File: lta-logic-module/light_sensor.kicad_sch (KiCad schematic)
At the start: 9 parts

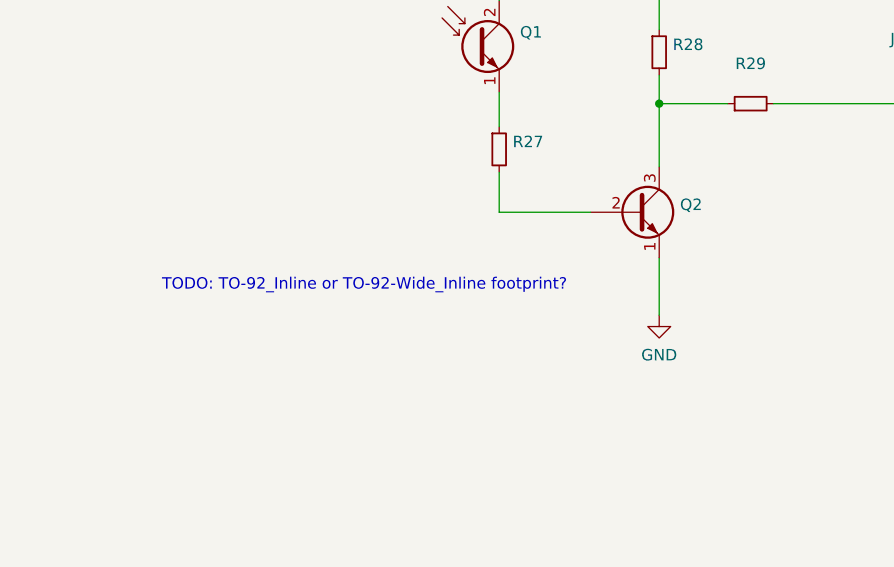
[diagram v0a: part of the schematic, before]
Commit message: Add main draft of PCB layout for logic module.
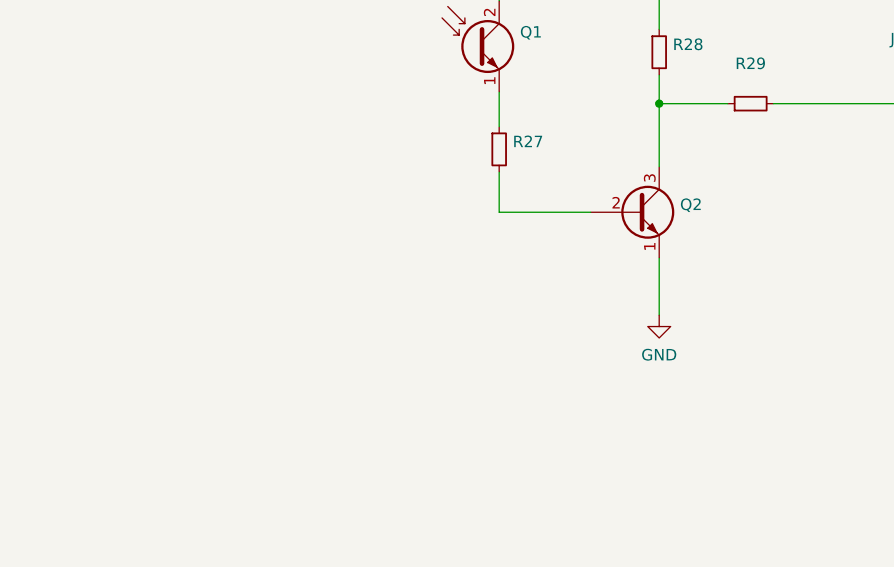
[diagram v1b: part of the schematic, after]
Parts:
- Q2: Comment (none) -> Any 2N3904 TO-92 transistor OK; MANUFACTURER onsemi -> Central Semiconductor; MPN KSC945CYTA -> 2N3904 PBFREE
- RV1: Comment (none) -> Any 25KOhm trimpot w/ same footprint OK
- SW1: Comment (none) -> Any 1x SPST THT dip switch w/ same footprint OK
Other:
- note removed: "TODO: TO-92_Inline or TO-92-Wide_Inline footprint?"
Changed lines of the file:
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@@
-    (effects (font (size 1.27 1.27)) (justify left bottom))
-  )
-  (text "TODO: TO-92_Inline or TO-92-Wide_Inline footprint?"
-    (at 36.83 76.835 0)
     (effects (font (size 1.27 1.27)) (justify left bottom))
   )
@@
     )
     (property "MANUFACTURER" "CUI Devices" (id 5) (at 122.555 34.925 90)
+      (effects (font (size 1.27 1.27)) hide)
+    )
+    (property "Comment" "Any 1x SPST THT dip switch w/ same footprint OK" (id 6) (at 122.555 34.925 0)
       (effects (font (size 1.27 1.27)) hide)
     )
@@
       (effects (font (size 1.27 1.27)) hide)
     )
-    (property "Datasheet" "https://www.onsemi.cn/pdf/datasheet/ksc945-d.pdf" (id 3) (at 89.535 67.945 0)
-      (effects (font (size 1.27 1.27)) hide)
-    )
-    (property "MPN" "KSC945CYTA" (id 4) (at 89.535 67.945 0)
-      (effects (font (size 1.27 1.27)) hide)
-    )
-    (property "MANUFACTURER" "onsemi" (id 5) (at 89.535 67.945 0)
+    (property "Datasheet" "" (id 3) (at 89.535 67.945 0)
+      (effects (font (size 1.27 1.27)) hide)
+    )
+    (property "MPN" "2N3904 PBFREE" (id 4) (at 89.535 67.945 0)
+      (effects (font (size 1.27 1.27)) hide)
+    )
+    (property "MANUFACTURER" "Central Semiconductor" (id 5) (at 89.535 67.945 0)
+      (effects (font (size 1.27 1.27)) hide)
+    )
+    (property "Comment" "Any 2N3904 TO-92 transistor OK" (id 6) (at 89.535 67.945 0)
       (effects (font (size 1.27 1.27)) hide)
     )
@@
   (symbol (lib_id "power:GND") (at 92.075 79.375 0) (unit 1)
     (in_bom yes) (on_board yes) (fields_autoplaced)
-    (property "Reference" "#PWR055" (id 0) (at 92.075 85.725 0)
+    (property "Reference" "#PWR056" (id 0) (at 92.075 85.725 0)
       (effects (font (size 1.27 1.27)) hide)
     )
@@
       (effects (font (size 1.27 1.27)) hide)
     )
+    (property "Comment" "Any 25KOhm trimpot w/ same footprint OK" (id 6) (at 92.075 40.005 0)
+      (effects (font (size 1.27 1.27)) hide)
+    )
     (pin "1")
     (pin "2")
@@
   (symbol (lib_id "power:GND") (at 31.115 28.575 0) (unit 1)
     (in_bom yes) (on_board yes) (fields_autoplaced)
-    (property "Reference" "#PWR054" (id 0) (at 31.115 34.925 0)
-      (effects (font (size 1.27 1.27)) hide)
-    )
+    (property "Reference" "#PWR055" (id 0) (at 31.115 34.925 0)
+      (effects (font (size 1.27 1.27)) hide)
+    )

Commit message: Re-establish symbol properties.
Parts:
- JP1: value (none) -> Jumper_3_Open
- SW1: value (none) -> SW_SPST
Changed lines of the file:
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@@
       (effects (font (size 1.27 1.27)) (justify right))
     )
-    (property "Value" "" (id 1) (at 123.698 36.6272 90)
+    (property "Value" "SW_SPST" (id 1) (at 123.698 36.6272 90)
       (effects (font (size 1.27 1.27)) (justify right))
     )
@@
       (effects (font (size 1.27 1.27)) (justify left))
     )
-    (property "Value" "" (id 1) (at 120.4209 51.2322 90)
+    (property "Value" "Jumper_3_Open" (id 1) (at 120.4209 51.2322 90)
       (effects (font (size 1.27 1.27)) (justify left))
     )

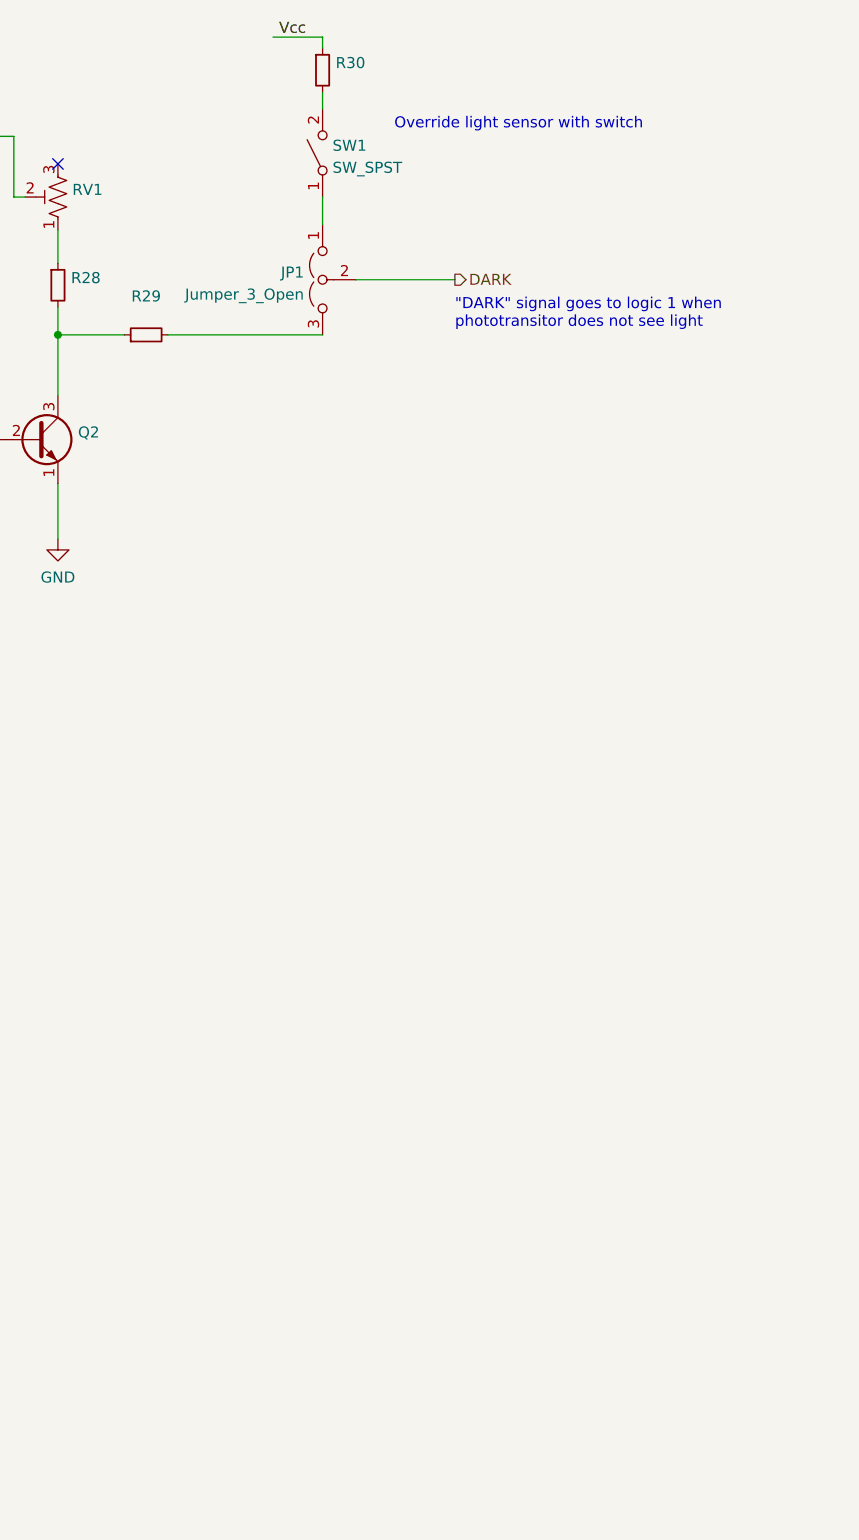
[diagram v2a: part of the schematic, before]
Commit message: Add test points
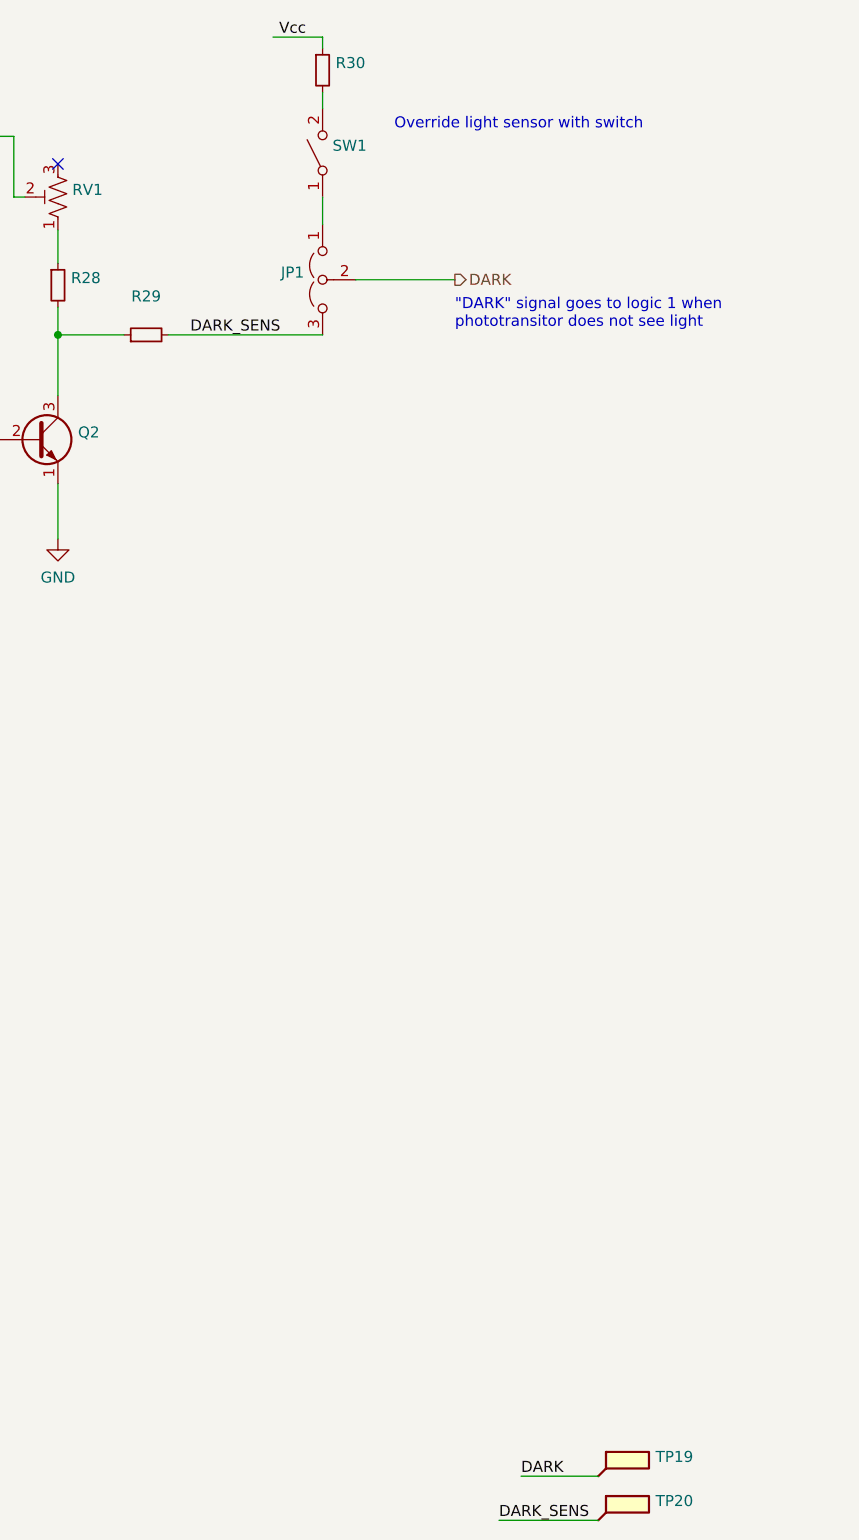
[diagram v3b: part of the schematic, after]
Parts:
- added TP19, TP20: (no value), symbol Connector:TestPoint_Flag
- JP1: value Jumper_3_Open -> (none)
- SW1: value SW_SPST -> (none)
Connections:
- net DARK: now also TP19.1
- net DARK_SENS: now reaches JP1.3 (B), R29.2
- net DARK_SENS: now also TP20.1
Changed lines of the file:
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@@
+    (stroke (width 0) (type default) (color 0 0 0 0))
+  )
+  (wire (pts (xy 145.415 187.325) (xy 154.305 187.325))
     (stroke (width 0) (type default) (color 0 0 0 0))
   )
@@
   )
   (wire (pts (xy 92.075 43.815) (xy 92.075 47.625))
+    (stroke (width 0) (type default) (color 0 0 0 0))
+  )
+  (wire (pts (xy 142.875 192.405) (xy 154.305 192.405))
     (stroke (width 0) (type default) (color 0 0 0 0))
   )
@@
     (effects (font (size 2.54 2.54)) (justify left bottom))
   )
+  (label "DARK" (at 145.415 187.325 0)
+    (effects (font (size 1.27 1.27)) (justify left bottom))
+  )
   (label "Vcc" (at 120.65 21.59 180)
     (effects (font (size 1.27 1.27)) (justify right bottom))
   )
+  (label "DARK_SENS" (at 107.315 55.88 0)
+    (effects (font (size 1.27 1.27)) (justify left bottom))
+  )
+  (label "DARK_SENS" (at 142.875 192.405 0)
+    (effects (font (size 1.27 1.27)) (justify left bottom))
+  )
   (label "Vcc" (at 72.39 33.02 180)
     (effects (font (size 1.27 1.27)) (justify right bottom))
@@
     (effects (font (size 1.27 1.27)) (justify right))
   )
+  (symbol (lib_id "Connector:TestPoint_Flag") (at 154.305 187.325 0) (unit 1)
+    (in_bom no) (on_board yes) (fields_autoplaced)
+    (property "Reference" "TP19" (id 0) (at 160.909 185.0933 0)
+      (effects (font (size 1.27 1.27)) (justify left))
+    )
+    (property "Value" "" (id 1) (at 160.909 187.6302 0)
+      (effects (font (size 1.27 1.27)) (justify left))
+    )
+    (property "Footprint" "" (id 2) (at 159.385 187.325 0)
+      (effects (font (size 1.27 1.27)) hide)
+    )
+    (property "Datasheet" "~" (id 3) (at 159.385 187.325 0)
+      (effects (font (size 1.27 1.27)) hide)
+    )
+    (pin "1")
+  )
   (symbol (lib_id "Switch:SW_SPST") (at 122.555 34.925 90) (unit 1)
     (in_bom yes) (on_board yes) (fields_autoplaced)
@@
       (effects (font (size 1.27 1.27)) (justify right))
     )
-    (property "Value" "SW_SPST" (id 1) (at 123.698 36.6272 90)
+    (property "Value" "" (id 1) (at 123.698 36.6272 90)
       (effects (font (size 1.27 1.27)) (justify right))
     )
@@
       (effects (font (size 1.27 1.27)) (justify left))
     )
-    (property "Value" "Jumper_3_Open" (id 1) (at 120.4209 51.2322 90)
+    (property "Value" "" (id 1) (at 120.4209 51.2322 90)
       (effects (font (size 1.27 1.27)) (justify left))
     )
@@
     (pin "2")
   )
+  (symbol (lib_id "Connector:TestPoint_Flag") (at 154.305 192.405 0) (unit 1)
+    (in_bom no) (on_board yes)
+    (property "Reference" "TP20" (id 0) (at 160.909 190.1733 0)
+      (effects (font (size 1.27 1.27)) (justify left))
+    )
+    (property "Value" "" (id 1) (at 161.29 192.405 0)
+      (effects (font (size 1.27 1.27)) (justify left))
+    )
+    (property "Footprint" "" (id 2) (at 159.385 192.405 0)
+      (effects (font (size 1.27 1.27)) hide)
+    )
+    (property "Datasheet" "~" (id 3) (at 159.385 192.405 0)
+      (effects (font (size 1.27 1.27)) hide)
+    )
+    (pin "1")
+  )
   (symbol (lib_id "Device:R_Potentiometer_Trim_US") (at 92.075 40.005 180) (unit 1)

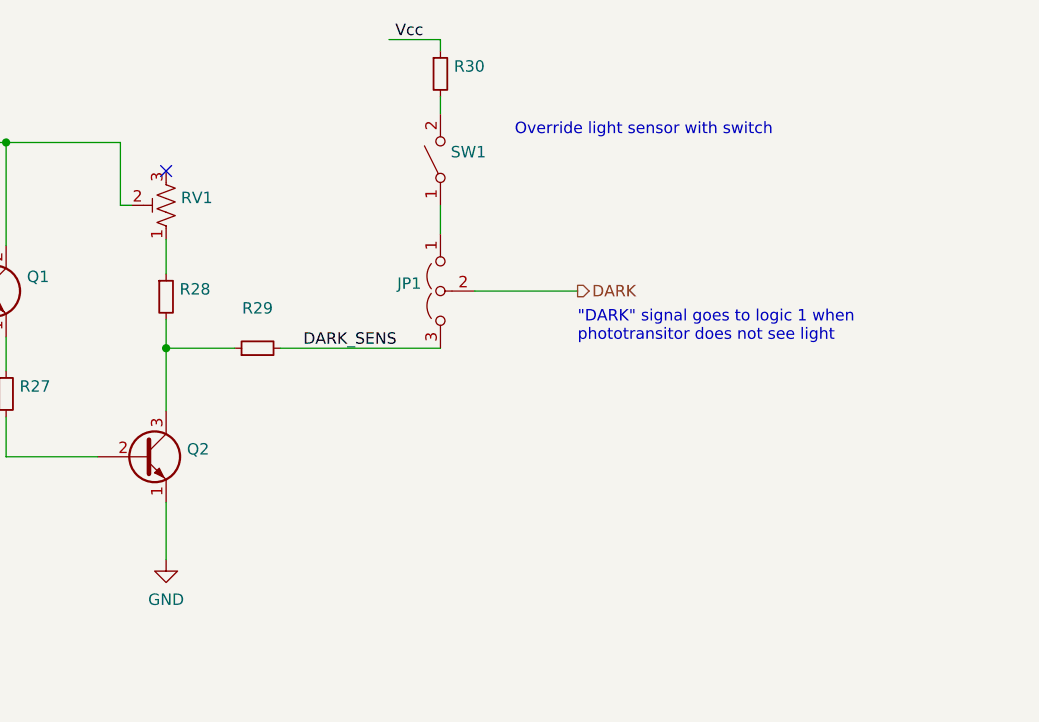
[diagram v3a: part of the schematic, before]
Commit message: Add indicator LED to SW1 enabled.
Adds 220K pull-down resistor to DARK signal. (Validated.)
Update solder thief pads and process direction indicator.
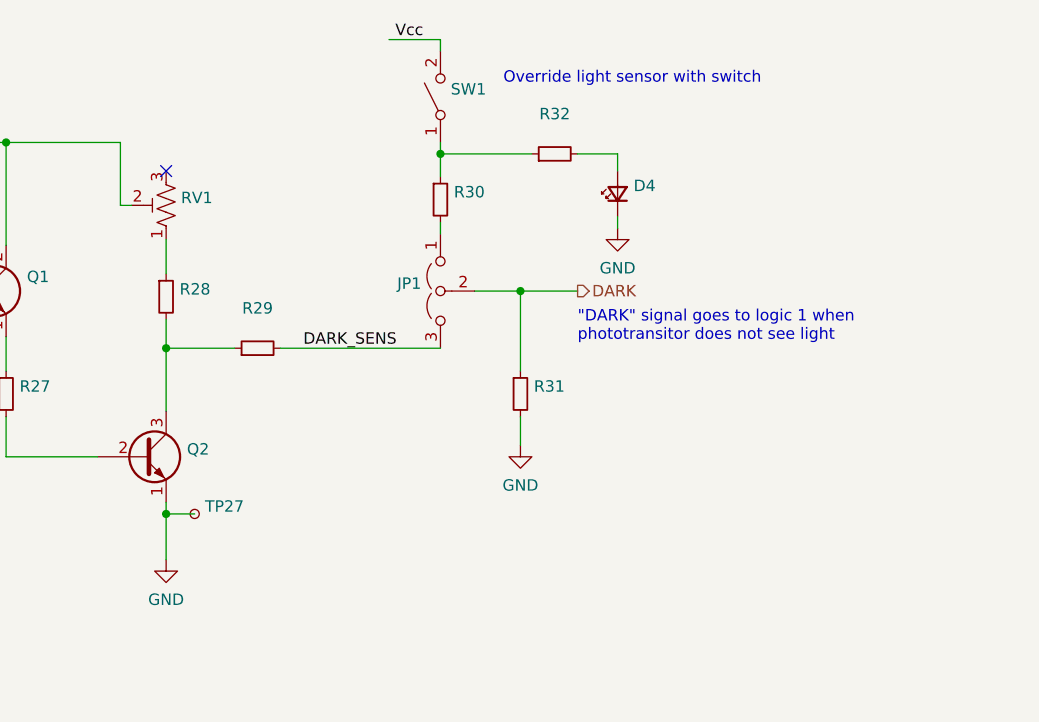
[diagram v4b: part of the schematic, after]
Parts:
- added D4: (no value), symbol Device:LED_Small
- added R31, R32: (no value), symbol Device:R_Small
- added TP27: (no value), symbol Connector:TestPoint_Small
- JP1: Comment Use 1x3 THT male pin header 2.54mm pitch -> Use 1x3 THT male pin header, gold mating, 2.54mm pitch
- Q1: Comment PT334 is externally-attached; mount 1x2 pin male header (2.54mm pitch) here -> PT334 is externally-attached; mount 1x2 pin male header (2.54mm pitch, gold) here
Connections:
- net DARK: now also R31.1
- net GND: now also D4.1 (K), R31.2, TP27.1
- net Vcc: now also SW1.2 (B); no longer R30.1
- net at SW1.1 (A): now also R30.1, R32.1; no longer JP1.1 (A)
- net at R30.2: now also JP1.1 (A); no longer SW1.2 (B)
- new net: D4.2 (A), R32.2
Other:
- moved on the sheet: R30, SW1

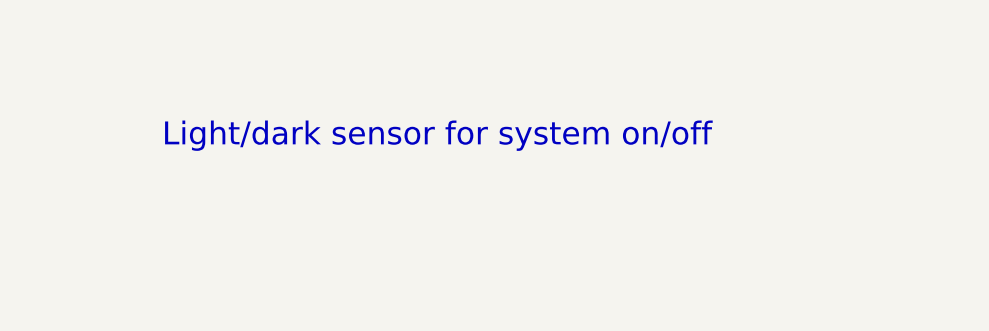
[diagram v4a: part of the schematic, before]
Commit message: Generate logic module 2022-05-08 v1.0 fab documentation.
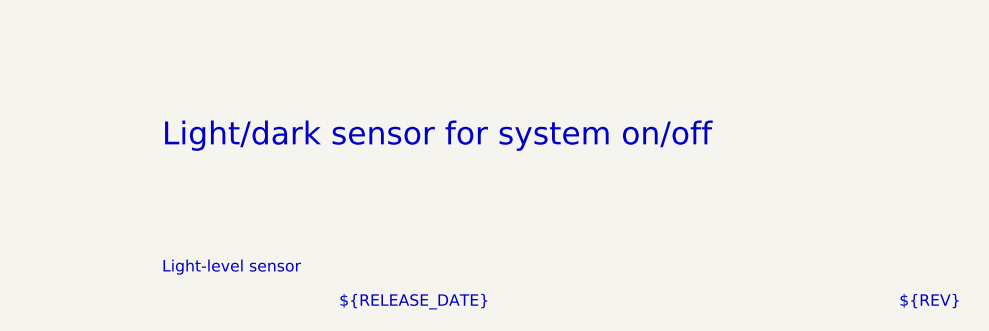
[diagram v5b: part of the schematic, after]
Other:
- note added: "${RELEASE_DATE}"
- note added: "${REV}"
- note added: "Light-level sensor"
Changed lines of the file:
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@@
     (stroke (width 0) (type default) (color 0 0 0 0))
+  )
+  (text "${REV}" (at 269.24 194.31 0)
+    (effects (font (size 1.27 1.27)) (justify left bottom))
   )
   (text "\"DARK\" signal goes to logic 1 when\nphototransitor does not see light"
@@
     (effects (font (size 1.27 1.27)) (justify left bottom))
   )
+  (text "Light-level sensor" (at 187.325 190.5 0)
+    (effects (font (size 1.27 1.27)) (justify left bottom))
+  )
   (text "Light/dark sensor for system on/off" (at 187.325 176.53 0)
     (effects (font (size 2.54 2.54)) (justify left bottom))
   )
+  (text "${RELEASE_DATE}" (at 207.01 194.31 0)
+    (effects (font (size 1.27 1.27)) (justify left bottom))
+  )
   (label "DARK" (at 145.415 187.325 0)
